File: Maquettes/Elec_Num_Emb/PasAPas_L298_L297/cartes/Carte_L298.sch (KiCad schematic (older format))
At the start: 19 parts, among them J1 Alim_MOT, J2 Commande_P, J3 TO_M1, J4 Commande_C, J5 Commande_CP, U1 L298HN, U2 L297

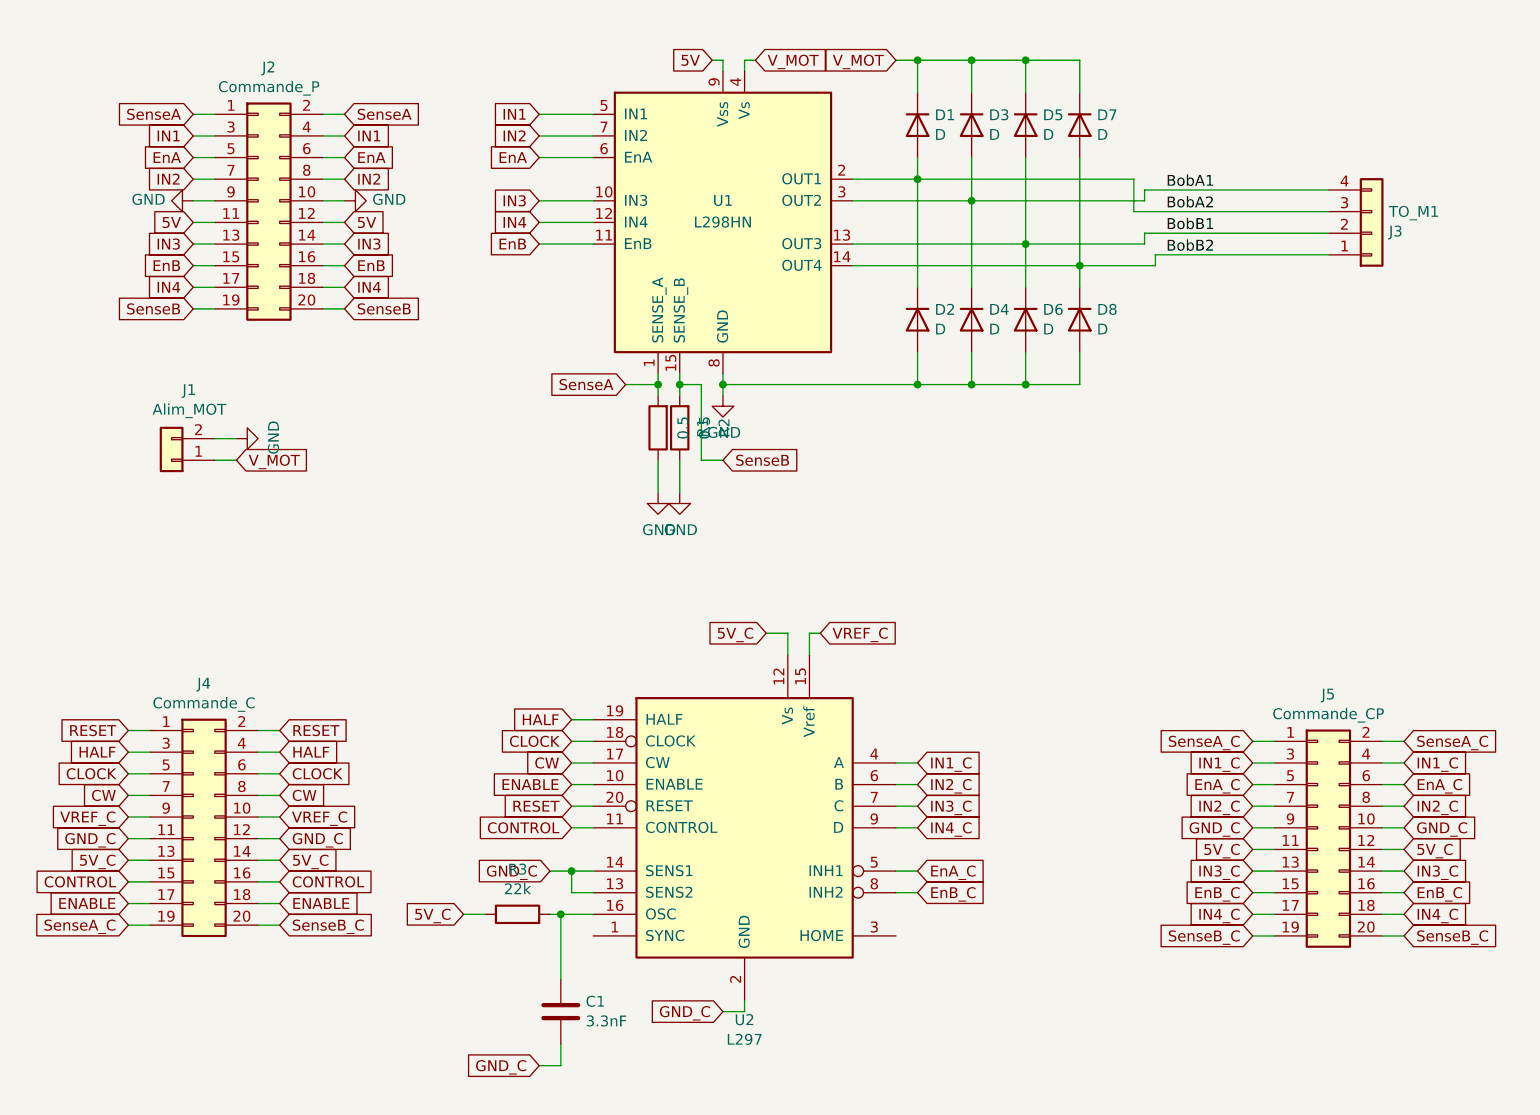
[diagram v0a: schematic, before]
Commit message: Mise à jour Maquette L297/L298 - Brochage
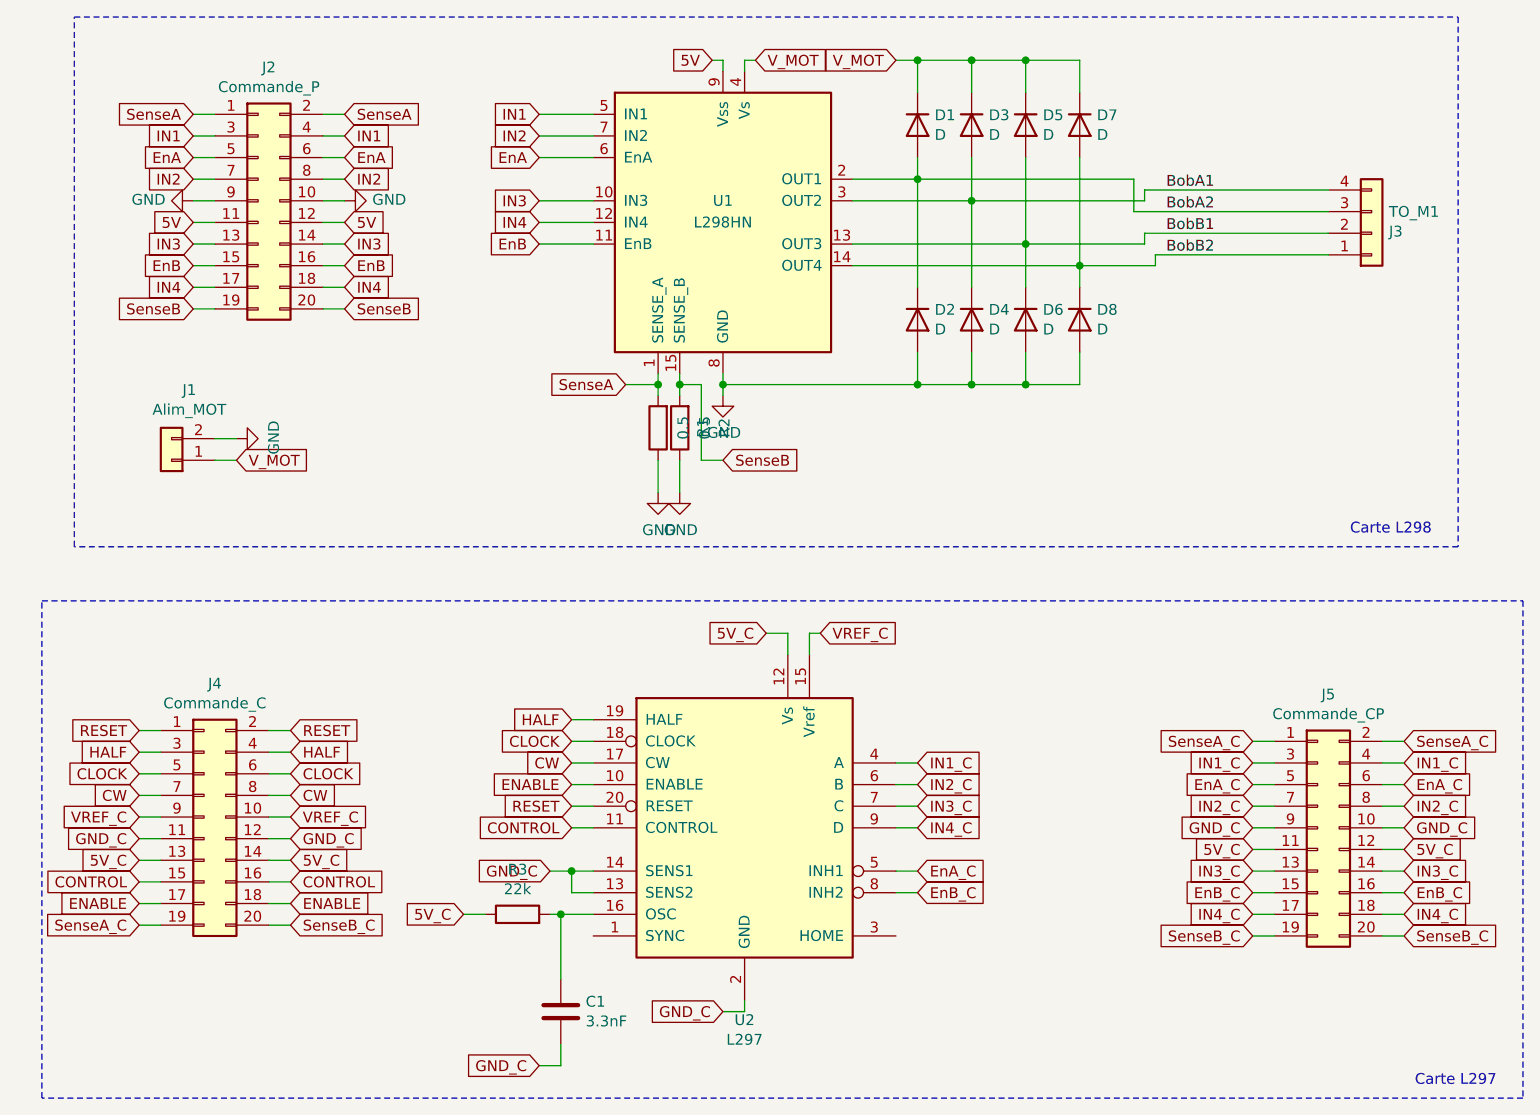
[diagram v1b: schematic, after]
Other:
- note added: "Carte L297"
- note added: "Carte L298"
- moved on the sheet: J4
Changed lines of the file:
@@
 EESchema Schematic File Version 4
-LIBS:Carte_L298-cache
-EELAYER 26 0
+EELAYER 30 0
 EELAYER END
 $Descr A4 11693 8268
@@
 L Connector_Generic:Conn_02x10_Odd_Even J4
 U 1 1 5FB7714A
-P 1400 4550
-F 0 "J4" H 1450 5167 50  0000 C CNN
-F 1 "Commande_C" H 1450 5076 50  0000 C CNN
-F 2 "Connector_PinHeader_2.54mm:PinHeader_2x10_P2.54mm_Vertical" H 1400 4550 50  0001 C CNN
-F 3 "~" H 1400 4550 50  0001 C CNN
-	1    1400 4550
+P 1450 4550
+F 0 "J4" H 1500 5167 50  0000 C CNN
+F 1 "Commande_C" H 1500 5076 50  0000 C CNN
+F 2 "Connector_PinHeader_2.54mm:PinHeader_2x10_P2.54mm_Vertical" H 1450 4550 50  0001 C CNN
+F 3 "~" H 1450 4550 50  0001 C CNN
+	1    1450 4550
 	1    0    0    -1
 $EndComp
@@
 Text GLabel 4750 4600 2    50   Input ~ 0
 IN4_C
-Text GLabel 1800 4250 2    50   Input ~ 0
+Text GLabel 1850 4250 2    50   Input ~ 0
 HALF
 Text GLabel 3150 4100 0    50   Input ~ 0
 HALF
-Text GLabel 1800 4350 2    50   Input ~ 0
+Text GLabel 1850 4350 2    50   Input ~ 0
 CLOCK
-Text GLabel 1800 4450 2    50   Input ~ 0
+Text GLabel 1850 4450 2    50   Input ~ 0
 CW
 Text GLabel 3150 4300 0    50   Input ~ 0
@@
 Text GLabel 4050 3700 0    50   Input ~ 0
 5V_C
-Text GLabel 1800 4650 2    50   Input ~ 0
+Text GLabel 1850 4650 2    50   Input ~ 0
 GND_C
-Text GLabel 1800 4750 2    50   Input ~ 0
+Text GLabel 1850 4750 2    50   Input ~ 0
 5V_C
-Text GLabel 1800 4550 2    50   Input ~ 0
+Text GLabel 1850 4550 2    50   Input ~ 0
 VREF_C
 Text GLabel 4300 3700 2    50   Input ~ 0
 VREF_C
-Text GLabel 1800 4850 2    50   Input ~ 0
+Text GLabel 1850 4850 2    50   Input ~ 0
 CONTROL
-Text GLabel 1800 4150 2    50   Input ~ 0
+Text GLabel 1850 4150 2    50   Input ~ 0
 RESET
-Text GLabel 1800 4950 2    50   Input ~ 0
+Text GLabel 1850 4950 2    50   Input ~ 0
 ENABLE
 Text GLabel 3150 4600 0    50   Input ~ 0
@@
 Text GLabel 3150 4400 0    50   Input ~ 0
 ENABLE
-Text GLabel 1100 4150 0    50   Input ~ 0
+Text GLabel 1150 4150 0    50   Input ~ 0
 RESET
-Text GLabel 1100 4250 0    50   Input ~ 0
+Text GLabel 1150 4250 0    50   Input ~ 0
 HALF
-Text GLabel 1100 4350 0    50   Input ~ 0
+Text GLabel 1150 4350 0    50   Input ~ 0
 CLOCK
-Text GLabel 1100 4450 0    50   Input ~ 0
+Text GLabel 1150 4450 0    50   Input ~ 0
 CW
-Text GLabel 1100 4550 0    50   Input ~ 0
+Text GLabel 1150 4550 0    50   Input ~ 0
 VREF_C
-Text GLabel 1100 4650 0    50   Input ~ 0
+Text GLabel 1150 4650 0    50   Input ~ 0
 GND_C
-Text GLabel 1100 4750 0    50   Input ~ 0
+Text GLabel 1150 4750 0    50   Input ~ 0
 5V_C
-Text GLabel 1100 4850 0    50   Input ~ 0
+Text GLabel 1150 4850 0    50   Input ~ 0
 CONTROL
-Text GLabel 1100 4950 0    50   Input ~ 0
+Text GLabel 1150 4950 0    50   Input ~ 0
 ENABLE
-Text GLabel 1800 5050 2    50   Input ~ 0
+Text GLabel 1850 5050 2    50   Input ~ 0
 SenseB_C
-Text GLabel 1100 5050 0    50   Input ~ 0
+Text GLabel 1150 5050 0    50   Input ~ 0
 SenseA_C
 Text GLabel 2650 5000 0    50   Input ~ 0
@@
 	3150 4600 3250 4600
 Wire Wire Line
-	1700 4150 1800 4150
-Wire Wire Line
-	1700 4250 1800 4250
-Wire Wire Line
-	1700 4350 1800 4350
-Wire Wire Line
-	1700 4450 1800 4450
-Wire Wire Line
-	1700 4550 1800 4550
-Wire Wire Line
-	1700 4650 1800 4650
-Wire Wire Line
-	1700 4750 1800 4750
-Wire Wire Line
-	1700 4850 1800 4850
-Wire Wire Line
-	1700 4950 1800 4950
-Wire Wire Line
-	1700 5050 1800 5050
-Wire Wire Line
-	1100 4150 1200 4150
-Wire Wire Line
-	1100 4250 1200 4250
-Wire Wire Line
-	1100 4350 1200 4350
-Wire Wire Line
-	1100 4450 1200 4450
-Wire Wire Line
-	1100 4550 1200 4550
-Wire Wire Line
-	1100 4650 1200 4650
-Wire Wire Line
-	1100 4750 1200 4750
-Wire Wire Line
-	1100 4850 1200 4850
-Wire Wire Line
-	1100 4950 1200 4950
-Wire Wire Line
-	1100 5050 1200 5050
+	1750 4150 1850 4150
+Wire Wire Line
+	1750 4250 1850 4250
+Wire Wire Line
+	1750 4350 1850 4350
+Wire Wire Line
+	1750 4450 1850 4450
+Wire Wire Line
+	1750 4550 1850 4550
+Wire Wire Line
+	1750 4650 1850 4650
+Wire Wire Line
+	1750 4750 1850 4750
+Wire Wire Line
+	1750 4850 1850 4850
+Wire Wire Line
+	1750 4950 1850 4950
+Wire Wire Line
+	1750 5050 1850 5050
+Wire Wire Line
+	1150 4150 1250 4150
+Wire Wire Line
+	1150 4250 1250 4250
+Wire Wire Line
+	1150 4350 1250 4350
+Wire Wire Line
+	1150 4450 1250 4450
+Wire Wire Line
+	1150 4550 1250 4550
+Wire Wire Line
+	1150 4650 1250 4650
+Wire Wire Line
+	1150 4750 1250 4750
+Wire Wire Line
+	1150 4850 1250 4850
+Wire Wire Line
+	1150 4950 1250 4950
+Wire Wire Line
+	1150 5050 1250 5050
+Wire Notes Line
+	850  850  7250 850
+Wire Notes Line
+	7250 850  7250 3300
+Wire Notes Line
+	7250 3300 850  3300
+Wire Notes Line
+	850  3300 850  850
+Text Notes 6750 3250 0    50   ~ 0
+Carte L298
+Wire Notes Line
+	700  3550 7550 3550
+Wire Notes Line
+	7550 3550 7550 5850
+Wire Notes Line
+	7550 5850 700  5850
+Wire Notes Line
+	700  5850 700  3550
+Text Notes 7050 5800 0    50   ~ 0
+Carte L297
 $EndSCHEMATC
